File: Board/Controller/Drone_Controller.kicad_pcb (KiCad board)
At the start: 2 copper layers, 71.1 x 134 mm, 7 parts, among them U1 NUCLEO144-H743ZI, U2 AT30TS74-XM8M-T, U3 ADF7020-1BCPZ, U4 QFN10_BMP581_BOS, U5 VL53L1CBV0FY-1, U6 LGA-14L_2P5X3X0P86_STM, U7 STM32F103C8Tx

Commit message: I have to update the suppository
Signed-off-by: EricTheGreat <joesmith01110000011101010111@gmail.com>
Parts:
- U3: renamed from U6; value LGA-14L_2P5X3X0P86_STM -> LSM6DSOTR
- U5: renamed from U4; value QFN10_BMP581_BOS -> BMP581
- U7: value STM32F103C8Tx -> SI4461-C2A-GMR; footprint Package_QFP:LQFP-48_7x7mm_P0.5mm -> KiCad_Cust:IC_SI4461-C2A-GMR
- moved U7 12.3 mm to (101.6, 98.4)
- renumbered U3 to U2, U5 to U4, U2 to U6

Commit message: we did stuff
Signed-off-by: EricTheGreat <joesmith01110000011101010111@gmail.com>
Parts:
- removed the U2 at (91.4, 71.1)
- removed U7: SI4461-C2A-GMR, KiCad_Cust:IC_SI4461-C2A-GMR
- added C1: .1uF, Resistor_SMD:R_0805_2012Metric, F.Cu at (93.3, 97.2)
- added C2: .1uF, Resistor_SMD:R_0805_2012Metric, F.Cu at (88.9, 97.2)
- renumbered U5 to U2, U4 to U3, U6 to U4, U3 to U5
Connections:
- U2 pad 1: unconnected-(U5-Pad1) (its old number) -> +3V3
- U2 pad 10: unconnected-(U5-Pad10) (its old number) -> +3V3
- U2 pad 2: unconnected-(U5-Pad2) (its old number) -> SPI1_SCK
- U2 pad 3: unconnected-(U5-Pad3) (its old number) -> GND
- U2 pad 4: unconnected-(U5-Pad4) (its old number) -> SPI1_MOSI
- U2 pad 5: unconnected-(U5-Pad5) (its old number) -> SPI1_MISO
- U2 pad 6: unconnected-(U5-Pad6) (its old number) -> SPI1_NSS
- U2 pad 7: unconnected-(U5-Pad7) (its old number) -> BMP_INT
- U2 pad 8: unconnected-(U5-Pad8) (its old number) -> GND
- U2 pad 9: unconnected-(U5-Pad9) (its old number) -> GND

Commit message: added connector
Signed-off-by: EricTheGreat <joesmith01110000011101010111@gmail.com>
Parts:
- added C3: .1uF, Resistor_SMD:R_0805_2012Metric, F.Cu at (99.7, 67.3)
- added C4: .1uF, Resistor_SMD:R_0805_2012Metric, F.Cu at (90.9, 67.3)
- added C5: .1uF, Resistor_SMD:R_0805_2012Metric, F.Cu at (90.9, 70.3)
- added R1: 2k, Resistor_SMD:R_0805_2012Metric, F.Cu at (95.3, 73.2)
- added R2: 2k, Resistor_SMD:R_0805_2012Metric, F.Cu at (95.3, 70.3)
- added R3: 2k, Resistor_SMD:R_0805_2012Metric, F.Cu at (95.3, 67.3)
- added R4: 2k, Resistor_SMD:R_0805_2012Metric, F.Cu at (90.9, 73.2)
- renumbered U5 to U4, U4 to U5
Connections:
- net BMP_INT renamed BMP_EXT
- U1 pad 21: unconnected-(U1-Pad21) -> I2C1_SDA
- U1 pad 32: unconnected-(U1-Pad32) -> SPI1_NSS
- U1 pad 35: unconnected-(U1-Pad35) -> SPI2_MISO
- U1 pad 45: unconnected-(U1-Pad45) -> SPI1_MOSI
- U1 pad 83: unconnected-(U1-Pad83) -> SPI1_SCK
- U1 pad 85: unconnected-(U1-Pad85) -> SPI1_MISO
- U1 pad 88: unconnected-(U1-Pad88) -> SPI2_NSS
- U1 pad 89: unconnected-(U1-Pad89) -> I2C1_SCL
- U1 pad 97: unconnected-(U1-Pad97) -> SPI2_SCK
- U1 pad 98: unconnected-(U1-Pad98) -> SPI2_MOSI
- U3 pad 1: unconnected-(U3-Pad1) -> +3V3
- U3 pad 10: unconnected-(U3-Pad10) -> I2C1_SCL
- U3 pad 11: unconnected-(U3-Pad11) -> +3V3
- U3 pad 12: unconnected-(U3-Pad12) -> GND
- U3 pad 2: unconnected-(U3-Pad2) -> GND
- U3 pad 3: unconnected-(U3-Pad3) -> GND
- U3 pad 4: unconnected-(U3-Pad4) -> GND
- U3 pad 5: unconnected-(U3-Pad5) -> Net-(R4-Pad1)
- U3 pad 6: unconnected-(U3-Pad6) -> GND
- U3 pad 7: unconnected-(U3-Pad7) -> LIDAR_EXT
- U3 pad 9: unconnected-(U3-Pad9) -> I2C1_SDA
- U4 pad 1: unconnected-(U5-Pad1) (its old number) -> SPI2_MISO
- U4 pad 12: unconnected-(U5-Pad12) -> SPI2_NSS
- U4 pad 13: unconnected-(U5-Pad13) -> SPI2_SCK
- U4 pad 14: unconnected-(U5-Pad14) -> SPI2_MOSI
- U4 pad 4: unconnected-(U5-Pad4) (its old number) -> IMU_EXT
- U4 pad 5: unconnected-(U5-Pad5) (its old number) -> +3V3
- U4 pad 6: unconnected-(U5-Pad6) (its old number) -> GND
- U4 pad 7: unconnected-(U5-Pad7) (its old number) -> GND
- U4 pad 8: unconnected-(U5-Pad8) (its old number) -> +3V3

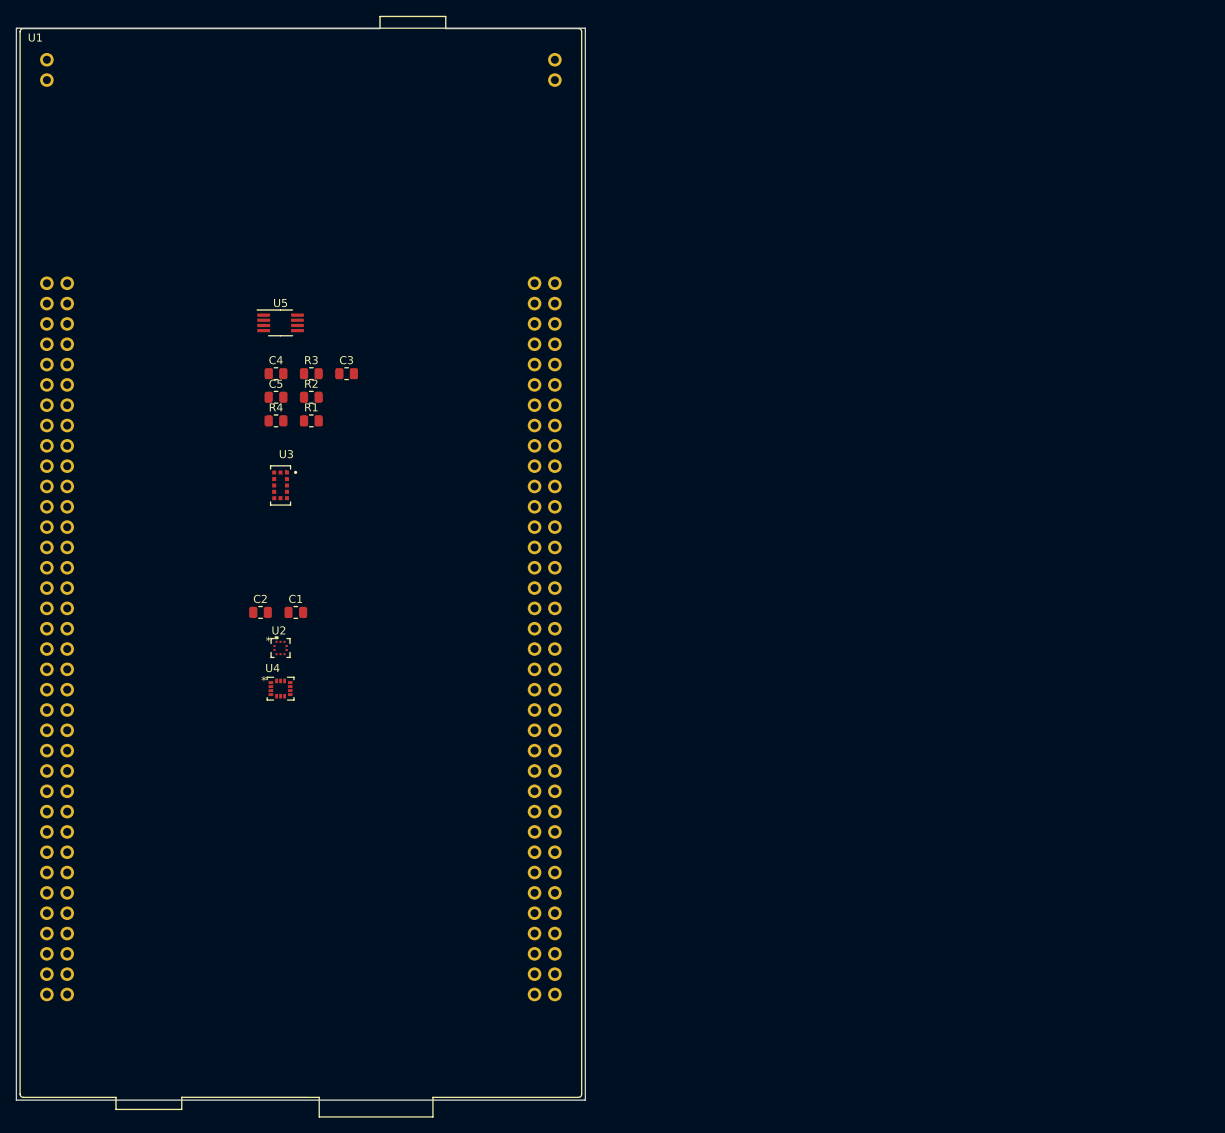
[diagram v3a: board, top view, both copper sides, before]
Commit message: added battery mux and LIDAR connectors
Signed-off-by: EricTheGreat <joesmith01110000011101010111@gmail.com>
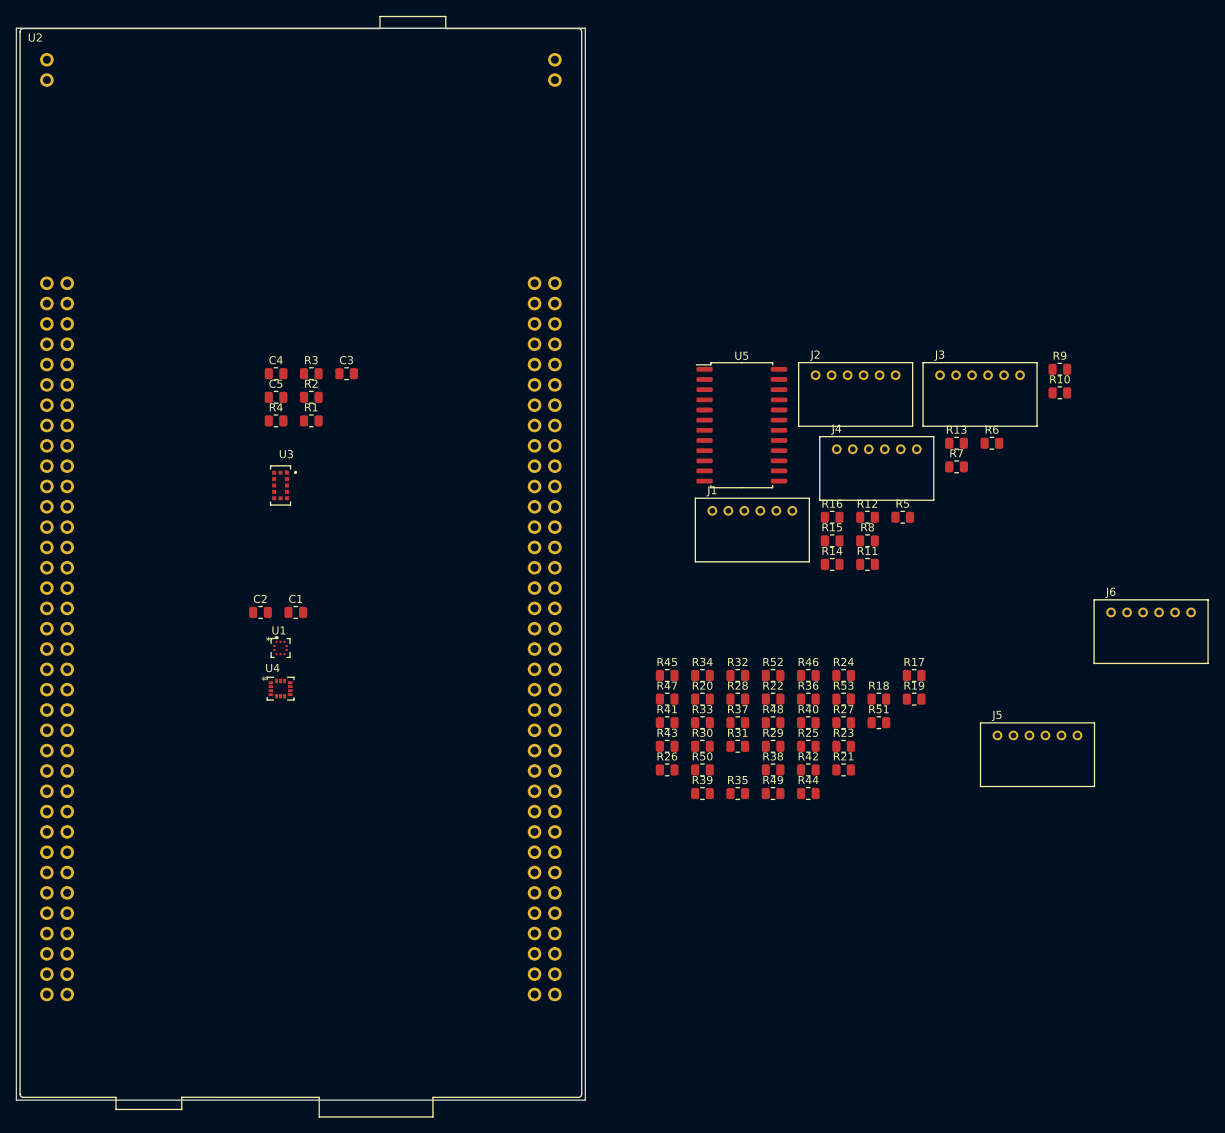
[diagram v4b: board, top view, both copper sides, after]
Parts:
- added J1: 140-506-415-000, KiCad_Cust:140-506-415-000, F.Cu at (145.4, 84.5)
- added J2: 140-506-415-000, KiCad_Cust:140-506-415-000, F.Cu at (158.3, 67.5)
- added J3: 140-506-415-000, KiCad_Cust:140-506-415-000, F.Cu at (173.9, 67.5)
- added J4: 140-506-415-000, KiCad_Cust:140-506-415-000, F.Cu at (161.0, 76.8)
- added J5: 140-506-415-000, KiCad_Cust:140-506-415-000, F.Cu at (181.1, 112.5)
- added J6: 140-506-415-000, KiCad_Cust:140-506-415-000, F.Cu at (195.3, 97.2)
- added R10: 2k, Resistor_SMD:R_0805_2012Metric, F.Cu at (188.9, 69.7)
- added R11: 2k, Resistor_SMD:R_0805_2012Metric, F.Cu at (164.8, 91.2)
- added R12: 2k, Resistor_SMD:R_0805_2012Metric, F.Cu at (164.8, 85.3)
- added R13: 2k, Resistor_SMD:R_0805_2012Metric, F.Cu at (175.9, 76.0)
- added R14: 2k, Resistor_SMD:R_0805_2012Metric, F.Cu at (160.4, 91.2)
- added R15: 2k, Resistor_SMD:R_0805_2012Metric, F.Cu at (160.4, 88.2)
- added R16: 2k, Resistor_SMD:R_0805_2012Metric, F.Cu at (160.4, 85.3)
- added R17: 1Meg, Resistor_SMD:R_0805_2012Metric, F.Cu at (170.6, 105.0)
- added R18: 68k, Resistor_SMD:R_0805_2012Metric, F.Cu at (166.2, 108.0)
- added R19: 4.7k, Resistor_SMD:R_0805_2012Metric, F.Cu at (170.6, 108.0)
- added R20: 1Meg, Resistor_SMD:R_0805_2012Metric, F.Cu at (144.2, 108.0)
- added R21: 47k, Resistor_SMD:R_0805_2012Metric, F.Cu at (161.8, 116.8)
- added R22: 33k, Resistor_SMD:R_0805_2012Metric, F.Cu at (153.0, 108.0)
- added R23: 1Meg, Resistor_SMD:R_0805_2012Metric, F.Cu at (161.8, 113.9)
- added R24: 100k, Resistor_SMD:R_0805_2012Metric, F.Cu at (161.8, 105.0)
- added R25: 1Meg, Resistor_SMD:R_0805_2012Metric, F.Cu at (157.4, 113.9)
- added R26: 1Meg, Resistor_SMD:R_0805_2012Metric, F.Cu at (139.8, 116.8)
- added R27: 100k, Resistor_SMD:R_0805_2012Metric, F.Cu at (161.8, 110.9)
- added R28: 3.3k, Resistor_SMD:R_0805_2012Metric, F.Cu at (148.6, 108.0)
- added R29: 1Meg, Resistor_SMD:R_0805_2012Metric, F.Cu at (153.0, 113.9)
- added R30: 100k, Resistor_SMD:R_0805_2012Metric, F.Cu at (144.2, 113.9)
- added R31: 22k, Resistor_SMD:R_0805_2012Metric, F.Cu at (148.6, 113.9)
- added R32: 1Meg, Resistor_SMD:R_0805_2012Metric, F.Cu at (148.6, 105.0)
- added R33: 100k, Resistor_SMD:R_0805_2012Metric, F.Cu at (144.2, 110.9)
- added R34: 47k, Resistor_SMD:R_0805_2012Metric, F.Cu at (144.2, 105.0)
- added R35: 1Meg, Resistor_SMD:R_0805_2012Metric, F.Cu at (148.6, 119.8)
- added R36: 150k, Resistor_SMD:R_0805_2012Metric, F.Cu at (157.4, 108.0)
- added R37: 6.8k, Resistor_SMD:R_0805_2012Metric, F.Cu at (148.6, 110.9)
- added R38: 1Meg, Resistor_SMD:R_0805_2012Metric, F.Cu at (153.0, 116.8)
- added R39: 100k, Resistor_SMD:R_0805_2012Metric, F.Cu at (144.2, 119.8)
- added R40: 100k, Resistor_SMD:R_0805_2012Metric, F.Cu at (157.4, 110.9)
- added R41: 1Meg, Resistor_SMD:R_0805_2012Metric, F.Cu at (139.8, 110.9)
- added R42: 470k, Resistor_SMD:R_0805_2012Metric, F.Cu at (157.4, 116.8)
- added R43: 680k, Resistor_SMD:R_0805_2012Metric, F.Cu at (139.8, 113.9)
- added R44: 1Meg, Resistor_SMD:R_0805_2012Metric, F.Cu at (157.4, 119.8)
- added R45: 300k, Resistor_SMD:R_0805_2012Metric, F.Cu at (139.8, 105.0)
- added R46: 3.3k, Resistor_SMD:R_0805_2012Metric, F.Cu at (157.4, 105.0)
- added R47: 1Meg, Resistor_SMD:R_0805_2012Metric, F.Cu at (139.8, 108.0)
- added R48: 270k, Resistor_SMD:R_0805_2012Metric, F.Cu at (153.0, 110.9)
- added R49: 330k, Resistor_SMD:R_0805_2012Metric, F.Cu at (153.0, 119.8)
- added R5: 2k, Resistor_SMD:R_0805_2012Metric, F.Cu at (169.2, 85.3)
- added R50: 1Meg, Resistor_SMD:R_0805_2012Metric, F.Cu at (144.2, 116.8)
- added R51: 1Meg, Resistor_SMD:R_0805_2012Metric, F.Cu at (166.2, 110.9)
- added R52: 1Meg, Resistor_SMD:R_0805_2012Metric, F.Cu at (153.0, 105.0)
- added R53: 1Meg, Resistor_SMD:R_0805_2012Metric, F.Cu at (161.8, 108.0)
- added R6: 2k, Resistor_SMD:R_0805_2012Metric, F.Cu at (180.4, 76.0)
- added R7: 2k, Resistor_SMD:R_0805_2012Metric, F.Cu at (175.9, 79.0)
- added R8: 2k, Resistor_SMD:R_0805_2012Metric, F.Cu at (164.8, 88.2)
- added R9: 2k, Resistor_SMD:R_0805_2012Metric, F.Cu at (188.9, 66.8)
- U5: value AT30TS74-XM8M-T -> CD74HC4067M; footprint Package_SO:MSOP-8_3x3mm_P0.65mm -> Package_SO:SOIC-24W_7.5x15.4mm_P1.27mm
- moved U5 59.1 mm to (149.1, 73.8)
- renumbered U2 to U1, U1 to U2
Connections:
- net LIDAR_EXT renamed LIDAR1_EXT
- R4 pad 2: GND -> +3V3
- U2 pad 122: unconnected-(U1-Pad122) -> I2C4_SCL
- U2 pad 132: unconnected-(U1-Pad132) -> I2C4_SDA
- U2 pad 2: unconnected-(U1-Pad2) -> I2C5_SCL
- U2 pad 51: unconnected-(U1-Pad51) -> I2C2_SCL
- U2 pad 53: unconnected-(U1-Pad53) -> I2C5_SDA
- U2 pad 73: unconnected-(U1-Pad73) -> I2C3_SDA
- U2 pad 90: unconnected-(U1-Pad90) -> I2C2_SDA
- U2 pad 95: unconnected-(U1-Pad95) -> I2C3_SCL
- U5 pad 2: unconnected-(U5-Pad2) -> V18
- U5 pad 3: unconnected-(U5-Pad3) -> V22
- U5 pad 4: unconnected-(U5-Pad4) -> V24
- U5 pad 5: unconnected-(U5-Pad5) -> V28
- U5 pad 6: unconnected-(U5-Pad6) -> V32
- U5 pad 7: unconnected-(U5-Pad7) -> V36
- U5 pad 8: unconnected-(U5-Pad8) -> V40
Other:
- copper layers 2 -> 4
